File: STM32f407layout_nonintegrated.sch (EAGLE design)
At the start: 45 parts, among them Q1 ASF, T3 FDN340P, T4 AP1117_LIN_REG

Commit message: Fixed some wrong info
fixed some stuff
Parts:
- R11, R12, R13, R14: value 83 -> 200
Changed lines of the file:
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@@
 <part name="+3V10" library="supply1" deviceset="+3V3" device=""/>
 <part name="C3" library="SparkFun-Passives" deviceset="CAP" device="0603-CAP" value="0.22uF"/>
-<part name="R11" library="SparkFun-Passives" deviceset="RESISTOR" device="0603-RES" value="83"/>
-<part name="R12" library="SparkFun-Passives" deviceset="RESISTOR" device="0603-RES" value="83"/>
-<part name="R13" library="SparkFun-Passives" deviceset="RESISTOR" device="0603-RES" value="83"/>
-<part name="R14" library="SparkFun-Passives" deviceset="RESISTOR" device="0603-RES" value="83"/>
+<part name="R11" library="SparkFun-Passives" deviceset="RESISTOR" device="0603-RES" value="200"/>
+<part name="R12" library="SparkFun-Passives" deviceset="RESISTOR" device="0603-RES" value="200"/>
+<part name="R13" library="SparkFun-Passives" deviceset="RESISTOR" device="0603-RES" value="200"/>
+<part name="R14" library="SparkFun-Passives" deviceset="RESISTOR" device="0603-RES" value="200"/>
 <part name="C8" library="SparkFun-Passives" deviceset="CAP" device="0603-CAP" value="4.7uF"/>
 <part name="GND15" library="supply1" deviceset="GND" device=""/>

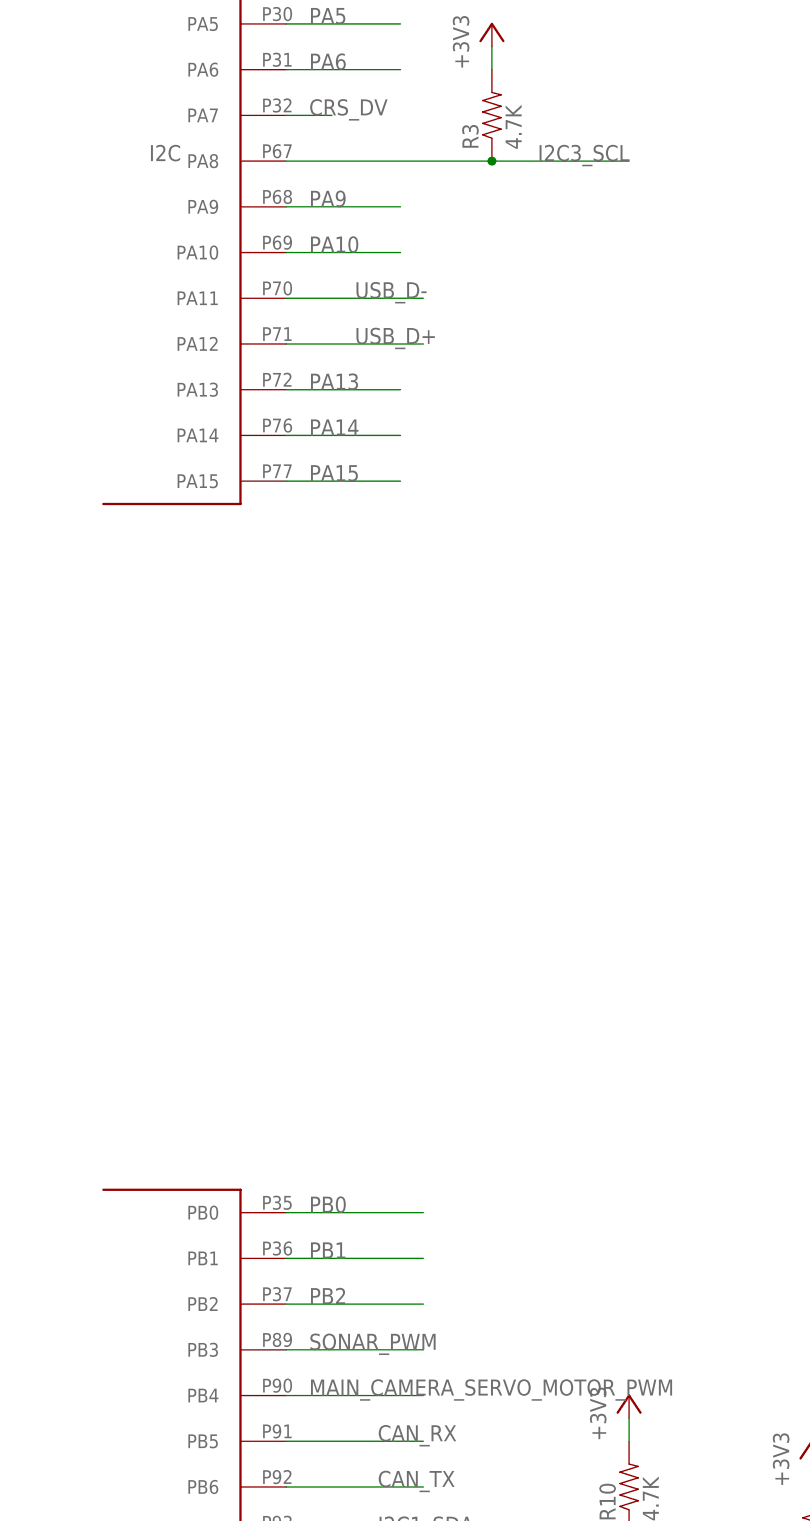
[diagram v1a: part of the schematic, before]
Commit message: Revision 2.0
Moved LED array, fixed pinout problems
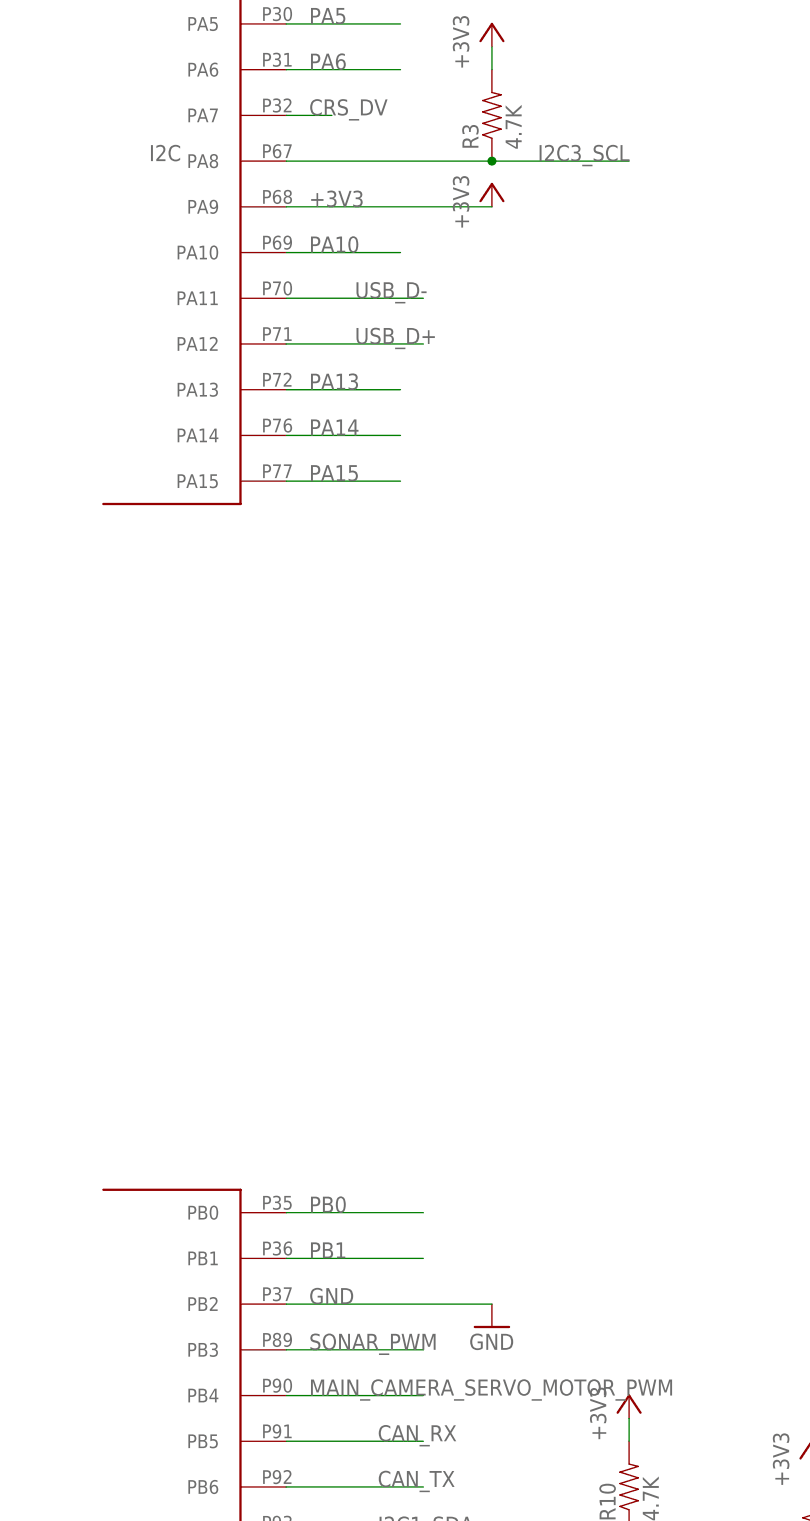
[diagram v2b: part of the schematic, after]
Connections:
- removed net PB2: U$1G$2.PB2
- net +3V3: now also U$1G$1.PA9
- net GND: now also U$1G$2.PB2
- net PA9: no longer U$1G$1.PA9
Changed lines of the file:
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@@
 <part name="P+1" library="supply1" deviceset="+5V" device=""/>
 <part name="JP1" library="Connectors" deviceset="M07" device=""/>
+<part name="GND4" library="SparkFun-Aesthetics" deviceset="GND" device=""/>
+<part name="+3V12" library="supply1" deviceset="+3V3" device=""/>
 </parts>
 <sheets>
@@
 <instance part="P+1" gate="1" x="441.96" y="147.32"/>
 <instance part="JP1" gate="G$1" x="472.44" y="187.96"/>
+<instance part="GND4" gate="1" x="462.28" y="340.36"/>
+<instance part="+3V12" gate="G$1" x="462.28" y="467.36"/>
 </instances>
 <busses>
@@
 <wire x1="477.52" y1="193.04" x2="485.14" y2="193.04" width="0.1524" layer="91"/>
 <label x="477.52" y="193.04" size="1.778" layer="95"/>
+</segment>
+<segment>
+<pinref part="U$1" gate="G$2" pin="PB2"/>
+<wire x1="439.42" y1="342.9" x2="462.28" y2="342.9" width="0.1524" layer="91"/>
+<label x="441.96" y="342.9" size="1.778" layer="95"/>
+<pinref part="GND4" gate="1" pin="GND"/>
 </segment>
 </net>
@@
 <label x="477.52" y="195.58" size="1.778" layer="95"/>
 </segment>
+<segment>
+<pinref part="U$1" gate="G$1" pin="PA9"/>
+<wire x1="439.42" y1="464.82" x2="462.28" y2="464.82" width="0.1524" layer="91"/>
+<label x="441.96" y="464.82" size="1.778" layer="95"/>
+<pinref part="+3V12" gate="G$1" pin="+3V3"/>
+</segment>
 </net>
 <net name="N$3" class="0">
@@
 <label x="406.4" y="246.38" size="1.778" layer="95"/>
 </segment>
-<segment>
-<pinref part="U$1" gate="G$1" pin="PA9"/>
-<wire x1="439.42" y1="464.82" x2="452.12" y2="464.82" width="0.1524" layer="91"/>
-<label x="441.96" y="464.82" size="1.778" layer="95"/>
-</segment>
 </net>
 <net name="PC7" class="0">
@@
 </segment>
 </net>
-<net name="PB2" class="0">
-<segment>
-<pinref part="U$1" gate="G$2" pin="PB2"/>
-<wire x1="439.42" y1="342.9" x2="454.66" y2="342.9" width="0.1524" layer="91"/>
-<label x="441.96" y="342.9" size="1.778" layer="95"/>
-</segment>
-</net>

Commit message: Fixed PA9 and routed
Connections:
- removed net N$57: T3.D, U$5.VCC
- removed net PA9: SV2.13
- new net USBPWR: SV2.13, T3.D, U$1G$1.PA9, U$5.VCC
- net +3V3: no longer U$1G$1.PA9
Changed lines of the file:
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@@
 <part name="JP1" library="Connectors" deviceset="M07" device=""/>
 <part name="GND4" library="SparkFun-Aesthetics" deviceset="GND" device=""/>
-<part name="+3V12" library="supply1" deviceset="+3V3" device=""/>
 </parts>
 <sheets>
@@
 <instance part="JP1" gate="G$1" x="472.44" y="187.96"/>
 <instance part="GND4" gate="1" x="462.28" y="340.36"/>
-<instance part="+3V12" gate="G$1" x="462.28" y="467.36"/>
 </instances>
 <busses>
@@
 <label x="477.52" y="195.58" size="1.778" layer="95"/>
 </segment>
-<segment>
-<pinref part="U$1" gate="G$1" pin="PA9"/>
-<wire x1="439.42" y1="464.82" x2="462.28" y2="464.82" width="0.1524" layer="91"/>
-<label x="441.96" y="464.82" size="1.778" layer="95"/>
-<pinref part="+3V12" gate="G$1" pin="+3V3"/>
-</segment>
 </net>
 <net name="N$3" class="0">
@@
 </segment>
 </net>
-<net name="N$57" class="0">
+<net name="USBPWR" class="0">
 <segment>
 <pinref part="U$5" gate="G$1" pin="VCC"/>
 <pinref part="T3" gate="A" pin="D"/>
-<wire x1="27.94" y1="78.74" x2="38.1" y2="78.74" width="0.1524" layer="91"/>
+<wire x1="27.94" y1="78.74" x2="30.48" y2="78.74" width="0.1524" layer="91"/>
+<wire x1="30.48" y1="78.74" x2="38.1" y2="78.74" width="0.1524" layer="91"/>
+<wire x1="30.48" y1="78.74" x2="30.48" y2="83.82" width="0.1524" layer="91"/>
+<junction x="30.48" y="78.74"/>
+<label x="30.48" y="81.28" size="1.778" layer="95" rot="R90"/>
+</segment>
+<segment>
+<pinref part="U$1" gate="G$1" pin="PA9"/>
+<wire x1="439.42" y1="464.82" x2="452.12" y2="464.82" width="0.1524" layer="91"/>
+<label x="449.58" y="464.82" size="1.778" layer="95"/>
+</segment>
+<segment>
+<pinref part="SV2" gate="G$1" pin="13"/>
+<wire x1="414.02" y1="246.38" x2="406.4" y2="246.38" width="0.1524" layer="91"/>
+<label x="406.4" y="246.38" size="1.778" layer="95"/>
 </segment>
 </net>
@@
 </segment>
 </net>
-<net name="PA9" class="0">
-<segment>
-<pinref part="SV2" gate="G$1" pin="13"/>
-<wire x1="414.02" y1="246.38" x2="406.4" y2="246.38" width="0.1524" layer="91"/>
-<label x="406.4" y="246.38" size="1.778" layer="95"/>
-</segment>
-</net>
